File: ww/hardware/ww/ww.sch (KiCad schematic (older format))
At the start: 45 parts

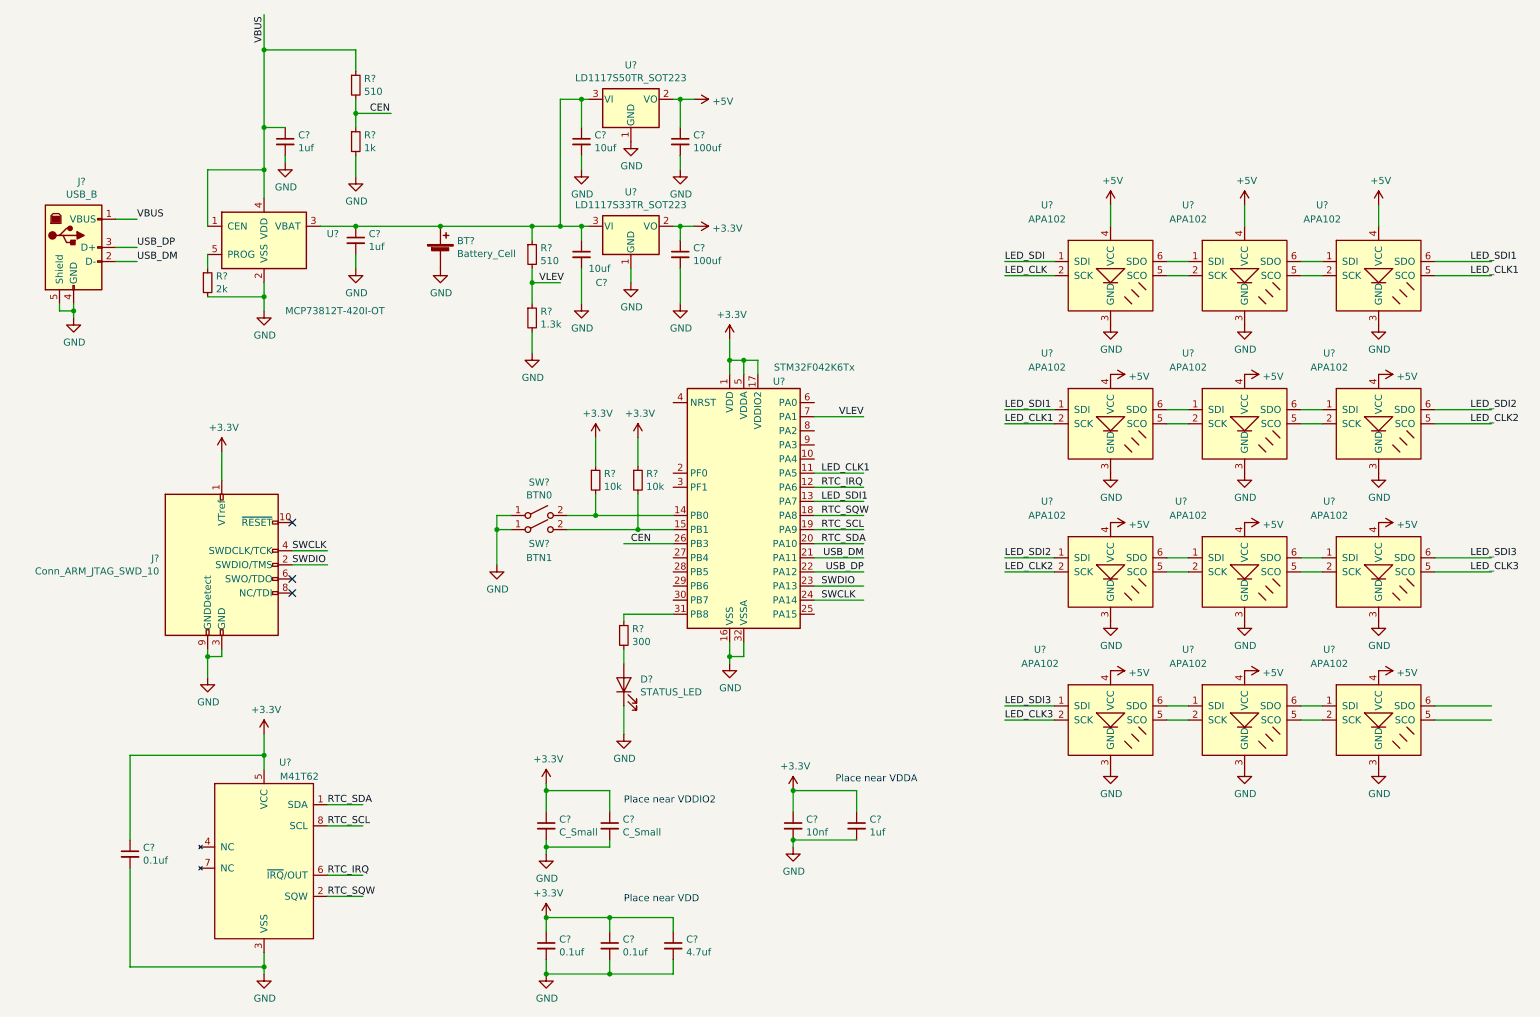
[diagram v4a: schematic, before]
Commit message: Fill out remaining footprint assignments
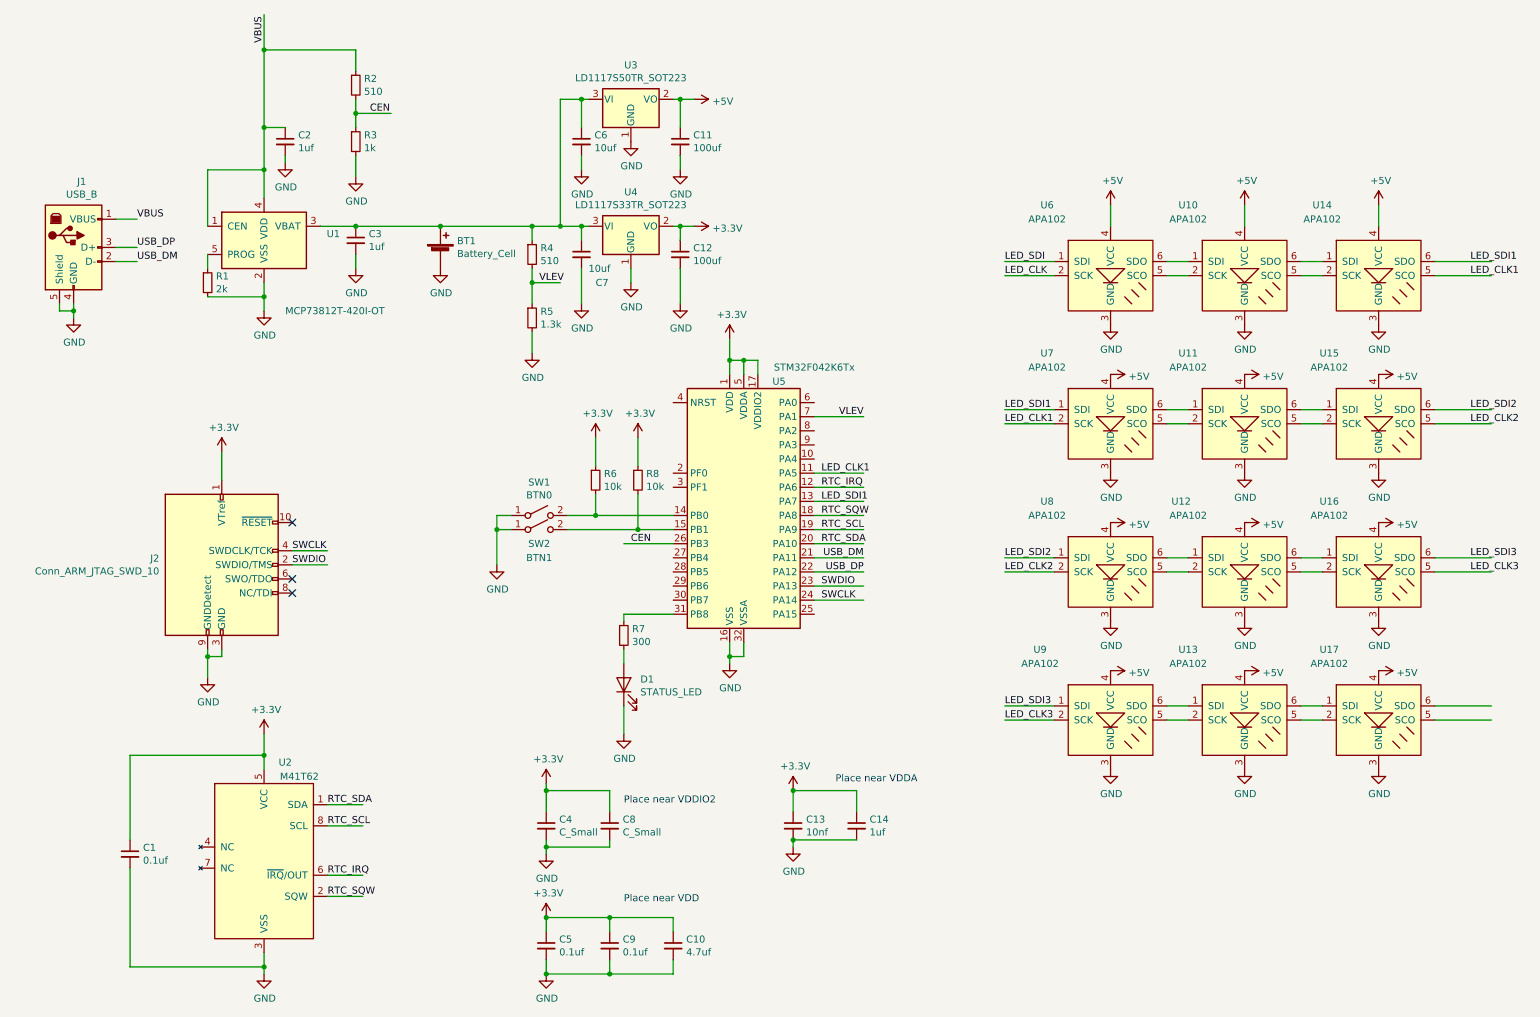
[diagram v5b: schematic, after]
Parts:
- BT1: renamed from BT?; footprint (none) -> Connectors_JST:JST_PH_B2B-PH-K_02x2.00mm_Straight
- C1, C10, C11, C12, C13, C14, C2, C3, C4, C5, C6, C7, C8, C9: renamed from C?; footprint (none) -> Capacitors_SMD:C_0603
- D1: renamed from D?; footprint (none) -> Diodes_SMD:D_0603
- J1: renamed from J?; footprint (none) -> Connectors_USB:USB_Micro-B_Molex-105017-0001
- J2: renamed from J?; footprint (none) -> Pin_Headers:Pin_Header_Straight_2x05_Pitch1.27mm_SMD
- R1, R2, R3, R4, R5, R6, R7, R8: renamed from R?; footprint (none) -> Resistors_SMD:R_0603
- SW1, SW2: renamed from SW?; footprint (none) -> Buttons_Switches_SMD:SW_SPST_EVQP0
- U10, U11, U12, U13, U14, U15, U16, U17, U6, U7, U8, U9: renamed from U?; footprint (none) -> ww:APA102-2020
- U2: renamed from U?; footprint (none) -> ww:PLCC-8_NoSilk
- gave numbers to parts that had none: 4

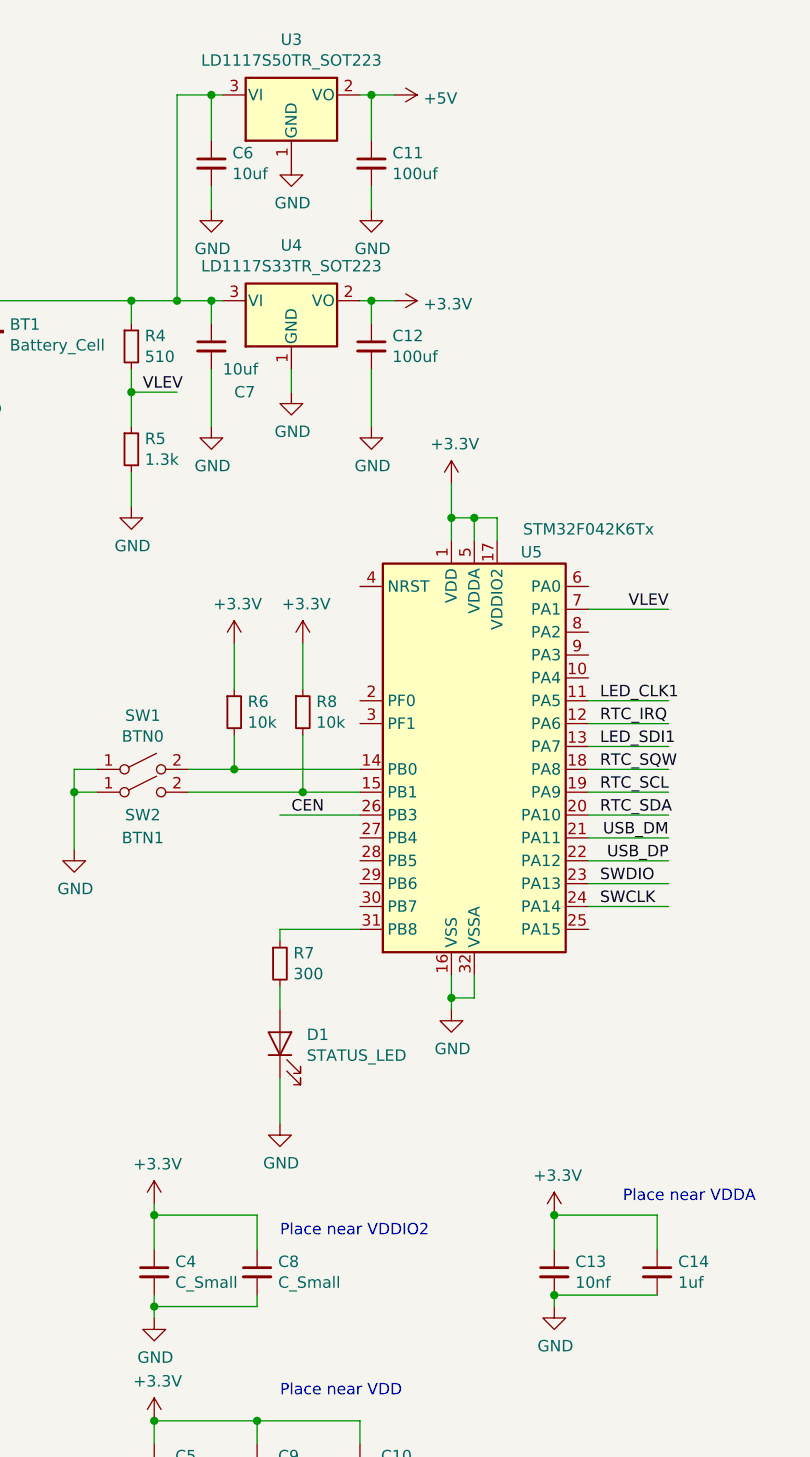
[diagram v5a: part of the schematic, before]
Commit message: Fill out more BOM items
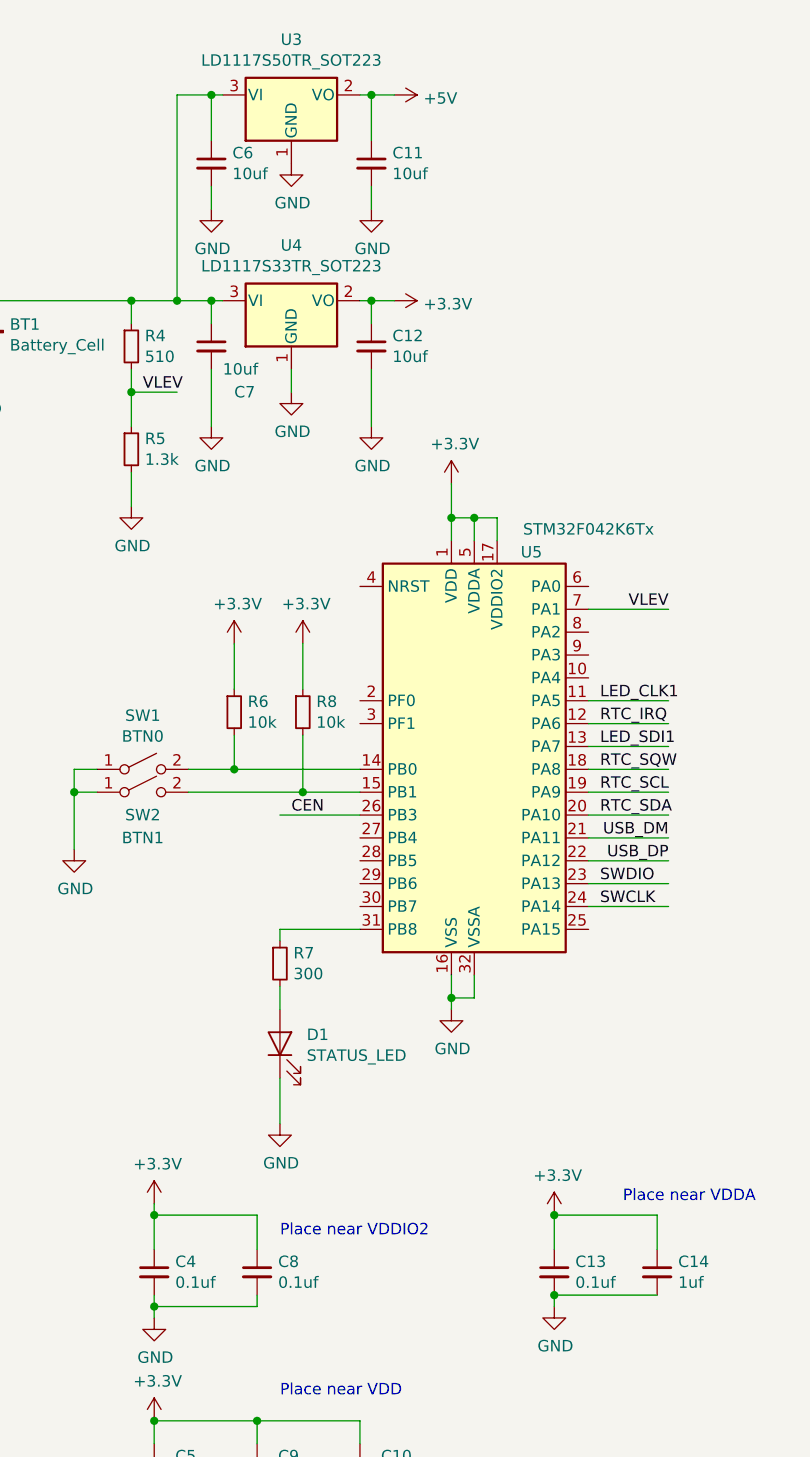
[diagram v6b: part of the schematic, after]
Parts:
- C11, C12: value 100uf -> 10uf
- C13: value 10nf -> 0.1uf
- C4, C8: value C_Small -> 0.1uf
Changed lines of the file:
@@
 P 4250 6350
 F 0 "C4" H 4342 6396 50  0000 L CNN
-F 1 "C_Small" H 4342 6305 50  0000 L CNN
+F 1 "0.1uf" H 4342 6305 50  0000 L CNN
 F 2 "Capacitors_SMD:C_0603" H 4250 6350 50  0001 C CNN
 F 3 "~" H 4250 6350 50  0001 C CNN
@@
 P 4700 6350
 F 0 "C8" H 4792 6396 50  0000 L CNN
-F 1 "C_Small" H 4792 6305 50  0000 L CNN
+F 1 "0.1uf" H 4792 6305 50  0000 L CNN
 F 2 "Capacitors_SMD:C_0603" H 4700 6350 50  0001 C CNN
 F 3 "~" H 4700 6350 50  0001 C CNN
@@
 P 6000 6350
 F 0 "C13" H 6092 6396 50  0000 L CNN
-F 1 "10nf" H 6092 6305 50  0000 L CNN
+F 1 "0.1uf" H 6092 6305 50  0000 L CNN
 F 2 "Capacitors_SMD:C_0603" H 6000 6350 50  0001 C CNN
 F 3 "~" H 6000 6350 50  0001 C CNN
@@
 P 5200 1500
 F 0 "C11" H 5292 1546 50  0000 L CNN
-F 1 "100uf" H 5292 1455 50  0000 L CNN
+F 1 "10uf" H 5292 1455 50  0000 L CNN
 F 2 "Capacitors_SMD:C_0603" H 5200 1500 50  0001 C CNN
 F 3 "~" H 5200 1500 50  0001 C CNN
@@
 P 5200 2300
 F 0 "C12" H 5292 2346 50  0000 L CNN
-F 1 "100uf" H 5292 2255 50  0000 L CNN
+F 1 "10uf" H 5292 2255 50  0000 L CNN
 F 2 "Capacitors_SMD:C_0603" H 5200 2300 50  0001 C CNN
 F 3 "~" H 5200 2300 50  0001 C CNN

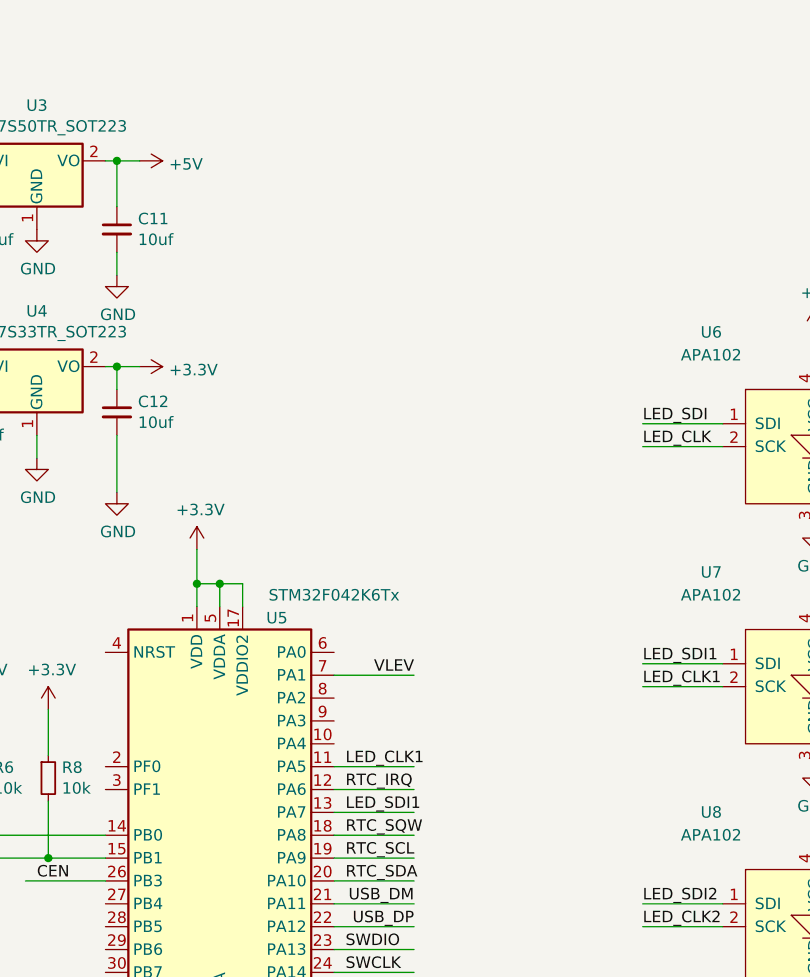
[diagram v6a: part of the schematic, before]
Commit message: Add test points
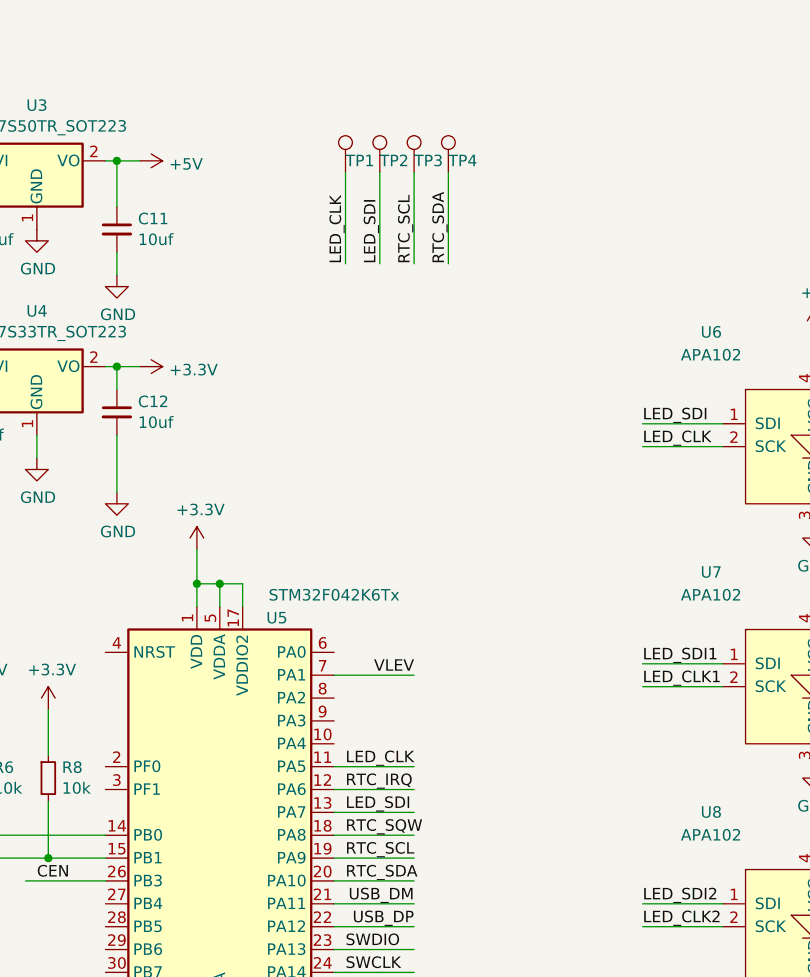
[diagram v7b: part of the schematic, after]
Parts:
- added TP1, TP2, TP3, TP4: TestPoint, Connectors_TestPoints:Test_Point_Pad_1.0x1.0mm, symbol Connector:TestPoint
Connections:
- wire segments 168 -> 172
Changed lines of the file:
@@
 	6150 3850 6500 3850
 Text Label 6200 3850 0    50   ~ 0
-LED_CLK1
+LED_CLK
 Wire Wire Line
 	6150 4050 6500 4050
 Text Label 6200 4050 0    50   ~ 0
-LED_SDI1
+LED_SDI
 $Comp
 L Connector:USB_B J1
@@
 Wire Wire Line
 	2250 600  2250 850
+$Comp
+L Connector:TestPoint TP1
+U 1 1 5DC79086
+P 6200 1250
+F 0 "TP1" H 6200 1300 50  0000 L CNN
+F 1 "TestPoint" H 5850 1550 50  0001 L CNN
+F 2 "Connectors_TestPoints:Test_Point_Pad_1.0x1.0mm" H 6400 1250 50  0001 C CNN
+F 3 "~" H 6400 1250 50  0001 C CNN
+	1    6200 1250
+	1    0    0    -1
+$EndComp
+Text Label 6200 1650 1    50   ~ 0
+LED_CLK
+Wire Wire Line
+	6200 1250 6200 1650
+$Comp
+L Connector:TestPoint TP2
+U 1 1 5DBEB3FA
+P 6350 1250
+F 0 "TP2" H 6350 1300 50  0000 L CNN
+F 1 "TestPoint" H 6408 1277 50  0001 L CNN
+F 2 "Connectors_TestPoints:Test_Point_Pad_1.0x1.0mm" H 6550 1250 50  0001 C CNN
+F 3 "~" H 6550 1250 50  0001 C CNN
+	1    6350 1250
+	1    0    0    -1
+$EndComp
+Wire Wire Line
+	6350 1250 6350 1650
+Text Label 6350 1650 1    50   ~ 0
+LED_SDI
+$Comp
+L Connector:TestPoint TP3
+U 1 1 5DBF4FBD
+P 6500 1250
+F 0 "TP3" H 6500 1300 50  0000 L CNN
+F 1 "TestPoint" H 6558 1277 50  0001 L CNN
+F 2 "Connectors_TestPoints:Test_Point_Pad_1.0x1.0mm" H 6700 1250 50  0001 C CNN
+F 3 "~" H 6700 1250 50  0001 C CNN
+	1    6500 1250
+	1    0    0    -1
+$EndComp
+Wire Wire Line
+	6500 1250 6500 1650
+Text Label 6500 1650 1    50   ~ 0
+RTC_SCL
+$Comp
+L Connector:TestPoint TP4
+U 1 1 5DBFFF5C
+P 6650 1250
+F 0 "TP4" H 6650 1300 50  0000 L CNN
+F 1 "TestPoint" H 6708 1277 50  0001 L CNN
+F 2 "Connectors_TestPoints:Test_Point_Pad_1.0x1.0mm" H 6850 1250 50  0001 C CNN
+F 3 "~" H 6850 1250 50  0001 C CNN
+	1    6650 1250
+	1    0    0    -1
+$EndComp
+Wire Wire Line
+	6650 1250 6650 1650
+Text Label 6650 1650 1    50   ~ 0
+RTC_SDA
 $EndSCHEMATC

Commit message: Initial major component PCB layout
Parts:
- U1: footprint Package_TO_SOT_SMD:SOT-23-5 -> TO_SOT_Packages_SMD:SOT-23-5
- U3, U4: footprint Package_TO_SOT_SMD:SOT-223-3_TabPin2 -> TO_SOT_Packages_SMD:SOT-223
- U5: footprint Package_QFP:LQFP-32_7x7mm_P0.8mm -> Housings_QFP:LQFP-32_7x7mm_Pitch0.8mm
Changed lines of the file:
@@
 F 0 "U5" H 5900 4900 50  0000 C CNN
 F 1 "STM32F042K6Tx" H 6150 5000 50  0000 C CNN
-F 2 "Package_QFP:LQFP-32_7x7mm_P0.8mm" H 5250 3150 50  0001 R CNN
+F 2 "Housings_QFP:LQFP-32_7x7mm_Pitch0.8mm" H 5250 3150 50  0001 R CNN
 F 3 "http://www.st.com/st-web-ui/static/active/en/resource/technical/document/datasheet/DM00105814.pdf" H 5650 4050 50  0001 C CNN
 	1    5650 4050
@@
 F 0 "U1" H 2694 2246 50  0000 L CNN
 F 1 "MCP73812T-420I-OT" H 2400 1700 50  0000 L CNN
-F 2 "Package_TO_SOT_SMD:SOT-23-5" H 2300 1950 50  0001 L CNN
+F 2 "TO_SOT_Packages_SMD:SOT-23-5" H 2300 1950 50  0001 L CNN
 F 3 "http://ww1.microchip.com/downloads/en/DeviceDoc/22036b.pdf" H 2000 2450 50  0001 C CNN
 	1    2250 2200
@@
 F 0 "U4" H 4850 2342 50  0000 C CNN
 F 1 "LD1117S33TR_SOT223" H 4850 2251 50  0000 C CNN
-F 2 "Package_TO_SOT_SMD:SOT-223-3_TabPin2" H 4850 2300 50  0001 C CNN
+F 2 "TO_SOT_Packages_SMD:SOT-223" H 4850 2300 50  0001 C CNN
 F 3 "http://www.st.com/st-web-ui/static/active/en/resource/technical/document/datasheet/CD00000544.pdf" H 4950 1850 50  0001 C CNN
 	1    4850 2100
@@
 F 0 "U3" H 4850 1442 50  0000 C CNN
 F 1 "LD1117S50TR_SOT223" H 4850 1351 50  0000 C CNN
-F 2 "Package_TO_SOT_SMD:SOT-223-3_TabPin2" H 4850 1400 50  0001 C CNN
+F 2 "TO_SOT_Packages_SMD:SOT-223" H 4850 1400 50  0001 C CNN
 F 3 "http://www.st.com/st-web-ui/static/active/en/resource/technical/document/datasheet/CD00000544.pdf" H 4950 950 50  0001 C CNN
 	1    4850 1200
